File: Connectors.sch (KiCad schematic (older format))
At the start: 12 parts, among them J1 Conn_01x06_Female, J2 Conn_01x04_Female, J4 Conn_01x06_Female, J5 Conn_01x06_Female, U3 74LVC2G86

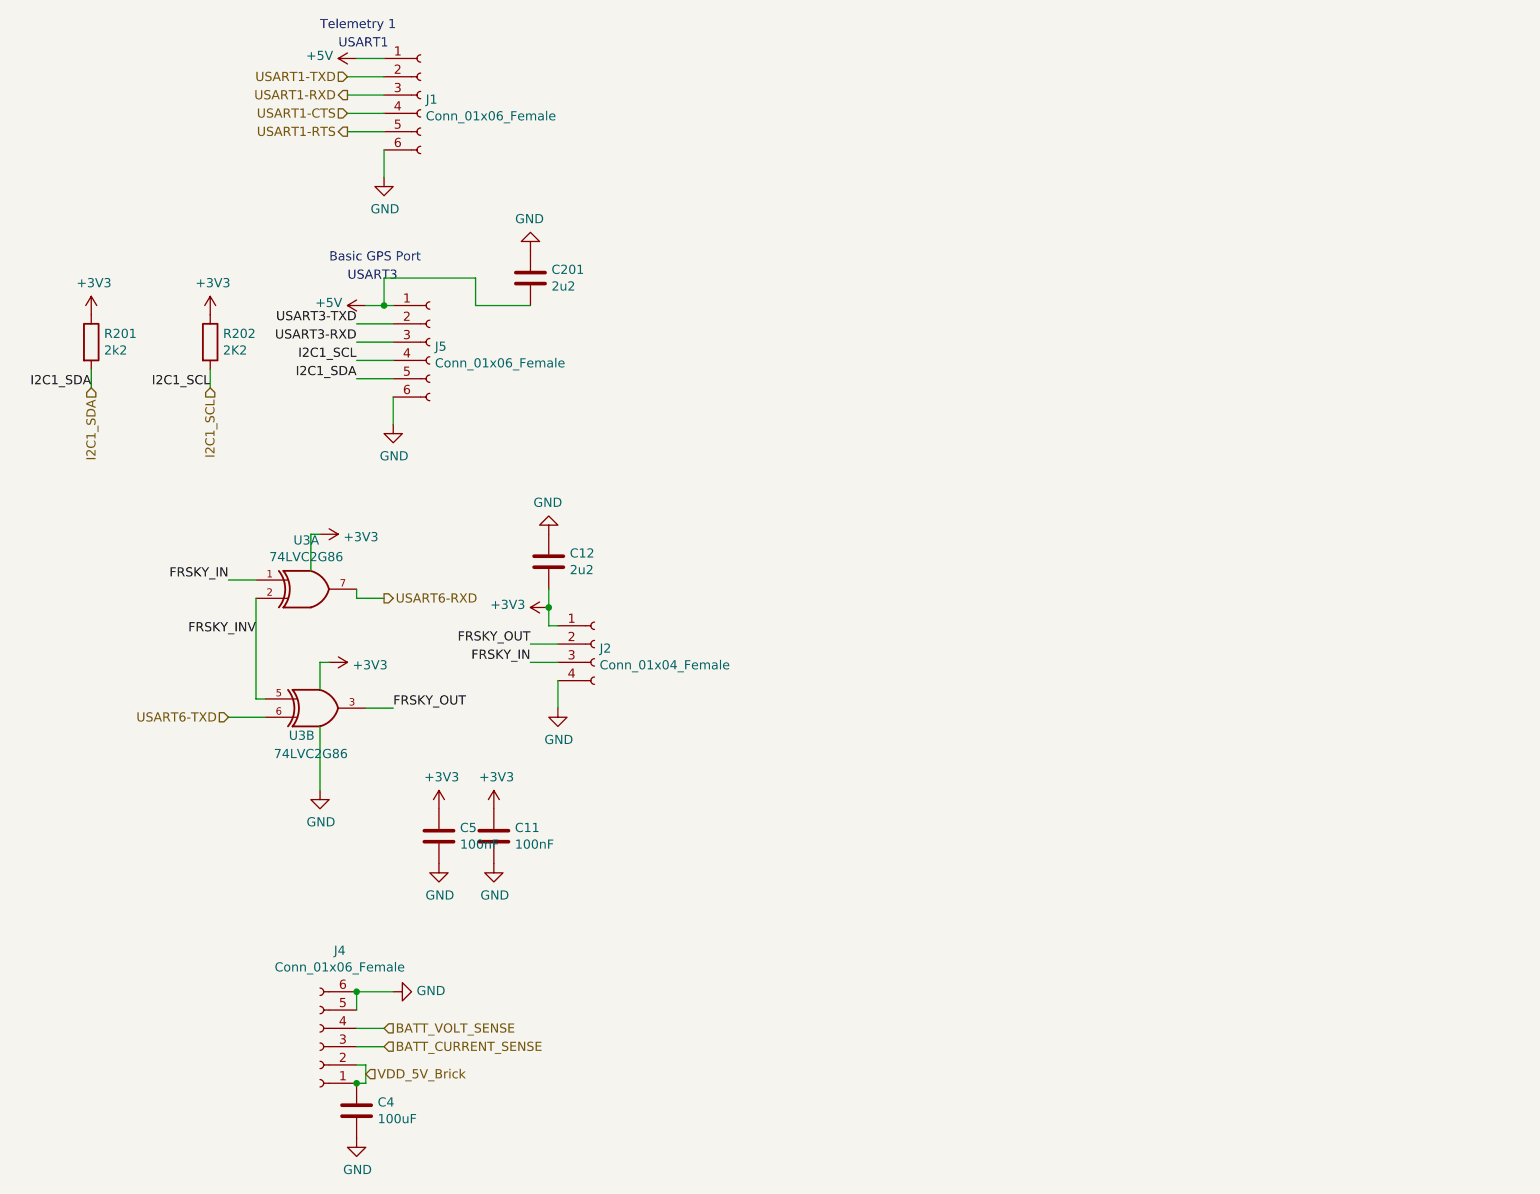
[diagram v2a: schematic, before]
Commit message: Added in Buzzer and N channel mosfet
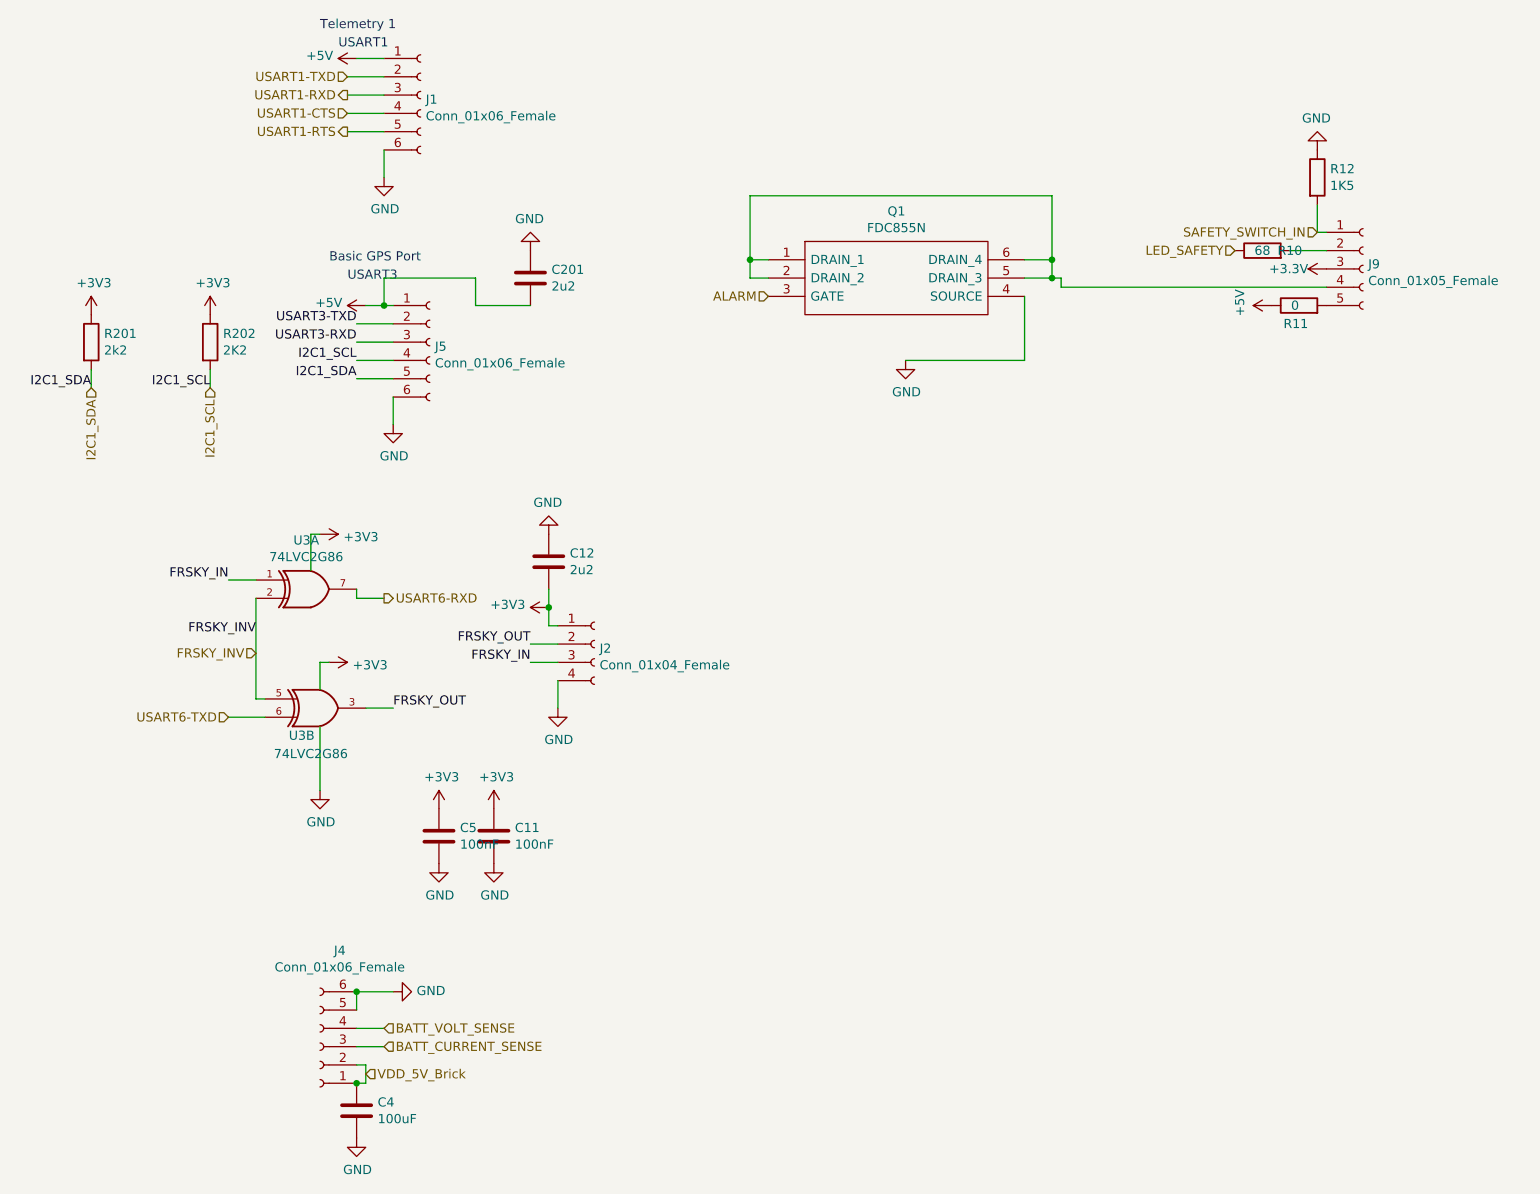
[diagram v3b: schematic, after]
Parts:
- added J9: Conn_01x05_Female, symbol Connector:Conn_01x05_Female
- added Q1: FDC855N, SOT95P280X110-6N, symbol SamacSys_Parts:FDC855N
- added R10: 68, symbol Device:R
- added R11: 0, symbol Device:R
- added R12: 1K5, Resistor_SMD:R_0603_1608Metric_Pad1.05x0.95mm_HandSolder, symbol Device:R
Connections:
- net +3V3: now also J9.3 (Pin_3)
- net +5V: now also R11.1
- net GND: now also Q1.4 (SOURCE), R12.1
- new net: J9.4 (Pin_4), Q1.1 (DRAIN_1), Q1.2 (DRAIN_2), Q1.5 (DRAIN_3), Q1.6 (DRAIN_4)
- new net: J9.2 (Pin_2), R10.2
- new net: J9.5 (Pin_5), R11.2
- new net ALARM: Q1.3 (GATE)
- new net LED_SAFETY: R10.1
- new net SAFETY_SWITCH_IN: J9.1 (Pin_1), R12.2
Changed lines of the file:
@@
 Text HLabel 2600 3900 2    50   Output ~ 0
 USART6-RXD
+Text HLabel 1900 4200 0    50   Input ~ 0
+FRSKY_INV
+$Comp
+L SamacSys_Parts:FDC855N Q1
+U 1 1 5ECF71A3
+P 4700 2050
+F 0 "Q1" H 5400 2315 50  0000 C CNN
+F 1 "FDC855N" H 5400 2224 50  0000 C CNN
+F 2 "SOT95P280X110-6N" H 5950 2150 50  0001 L CNN
+F 3 "http://docs-asia.electrocomponents.com/webdocs/12cf/0900766b812cf73c.pdf" H 5950 2050 50  0001 L CNN
+F 4 "Fairchild FDC855N N-channel MOSFET Transistor, 6.1 A, 30 V, 6-Pin SOT-23" H 5950 1950 50  0001 L CNN "Description"
+F 5 "1.1" H 5950 1850 50  0001 L CNN "Height"
+F 6 "ON Semiconductor" H 5950 1750 50  0001 L CNN "Manufacturer_Name"
+F 7 "FDC855N" H 5950 1650 50  0001 L CNN "Manufacturer_Part_Number"
+F 8 "512-FDC855N" H 5950 1550 50  0001 L CNN "Mouser Part Number"
+F 9 "https://www.mouser.co.uk/ProductDetail/ON-Semiconductor-Fairchild/FDC855N?qs=sXL1QONaU64rYBwsoFljaQ%3D%3D" H 5950 1450 50  0001 L CNN "Mouser Price/Stock"
+F 10 "8090871P" H 5950 1350 50  0001 L CNN "RS Part Number"
+F 11 "http://uk.rs-online.com/web/p/products/8090871P" H 5950 1250 50  0001 L CNN "RS Price/Stock"
+	1    4700 2050
+	1    0    0    -1
+$EndComp
+$Comp
+L Connector:Conn_01x05_Female J9
+U 1 1 5ECF887A
+P 7950 2100
+F 0 "J9" H 7978 2126 50  0000 L CNN
+F 1 "Conn_01x05_Female" H 7978 2035 50  0000 L CNN
+F 2 "" H 7950 2100 50  0001 C CNN
+F 3 "~" H 7950 2100 50  0001 C CNN
+	1    7950 2100
+	1    0    0    -1
+$EndComp
+Wire Wire Line
+	7750 1900 7700 1900
+Wire Wire Line
+	7700 1900 7700 1750
+$Comp
+L Device:R R12
+U 1 1 5ECFBF90
+P 7700 1600
+F 0 "R12" H 7770 1646 50  0000 L CNN
+F 1 "1K5" H 7770 1555 50  0000 L CNN
+F 2 "Resistor_SMD:R_0603_1608Metric_Pad1.05x0.95mm_HandSolder" V 7630 1600 50  0001 C CNN
+F 3 "~" H 7700 1600 50  0001 C CNN
+	1    7700 1600
+	1    0    0    -1
+$EndComp
+$Comp
+L power:GND #PWR032
+U 1 1 5ECFC690
+P 7700 1450
+F 0 "#PWR032" H 7700 1200 50  0001 C CNN
+F 1 "GND" H 7705 1277 50  0000 C CNN
+F 2 "" H 7700 1450 50  0001 C CNN
+F 3 "" H 7700 1450 50  0001 C CNN
+	1    7700 1450
+	-1   0    0    1
+$EndComp
+Text HLabel 7700 1900 0    50   Input ~ 0
+SAFETY_SWITCH_IN
+$Comp
+L Device:R R10
+U 1 1 5ECFE4AF
+P 7400 2000
+F 0 "R10" V 7400 1850 50  0000 C CNN
+F 1 "68" V 7400 2000 50  0000 C CNN
+F 2 "" V 7330 2000 50  0001 C CNN
+F 3 "~" H 7400 2000 50  0001 C CNN
+	1    7400 2000
+	0    -1   -1   0
+$EndComp
+Wire Wire Line
+	7750 2000 7550 2000
+Text HLabel 7250 2000 0    50   Input ~ 0
+LED_SAFETY
+$Comp
+L power:+3.3V #PWR033
+U 1 1 5ED00DDC
+P 7750 2100
+F 0 "#PWR033" H 7750 1950 50  0001 C CNN
+F 1 "+3.3V" V 7750 2200 50  0000 L CNN
+F 2 "" H 7750 2100 50  0001 C CNN
+F 3 "" H 7750 2100 50  0001 C CNN
+	1    7750 2100
+	0    -1   -1   0
+$EndComp
+$Comp
+L power:GND #PWR030
+U 1 1 5ED01AAB
+P 5450 2600
+F 0 "#PWR030" H 5450 2350 50  0001 C CNN
+F 1 "GND" H 5455 2427 50  0000 C CNN
+F 2 "" H 5450 2600 50  0001 C CNN
+F 3 "" H 5450 2600 50  0001 C CNN
+	1    5450 2600
+	1    0    0    -1
+$EndComp
+$Comp
+L power:+5V #PWR031
+U 1 1 5ED02565
+P 7450 2300
+F 0 "#PWR031" H 7450 2150 50  0001 C CNN
+F 1 "+5V" H 7465 2473 50  0000 C CNN
+F 2 "" H 7450 2300 50  0001 C CNN
+F 3 "" H 7450 2300 50  0001 C CNN
+	1    7450 2300
+	0    -1   -1   0
+$EndComp
+$Comp
+L Device:R R11
+U 1 1 5ED03190
+P 7600 2300
+F 0 "R11" V 7500 2250 50  0000 L CNN
+F 1 "0" V 7600 2300 50  0000 L CNN
+F 2 "" V 7530 2300 50  0001 C CNN
+F 3 "~" H 7600 2300 50  0001 C CNN
+	1    7600 2300
+	0    -1   -1   0
+$EndComp
+Wire Wire Line
+	6100 2150 6250 2150
+Wire Wire Line
+	6300 2150 6300 2200
+Wire Wire Line
+	6250 2150 6250 2050
+Wire Wire Line
+	6250 2050 6100 2050
+Connection ~ 6250 2150
+Wire Wire Line
+	6250 2150 6300 2150
+Wire Wire Line
+	4700 2150 4600 2150
+Wire Wire Line
+	4600 2150 4600 2050
+Wire Wire Line
+	4600 2050 4700 2050
+Wire Wire Line
+	4600 2050 4600 1700
+Wire Wire Line
+	4600 1700 6250 1700
+Wire Wire Line
+	6250 1700 6250 2050
+Connection ~ 4600 2050
+Connection ~ 6250 2050
+Wire Wire Line
+	6100 2250 6100 2600
+Wire Wire Line
+	6100 2600 5450 2600
+Wire Wire Line
+	6300 2200 7750 2200
+Text HLabel 4700 2250 0    50   Input ~ 0
+ALARM
 $EndSCHEMATC
